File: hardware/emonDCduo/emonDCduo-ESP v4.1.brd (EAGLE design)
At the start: 114.3 x 76.5 mm, 120 parts, among them IC1 ACS750LCA-050, IC2 ACS750LCA-050, Y1 32Khz

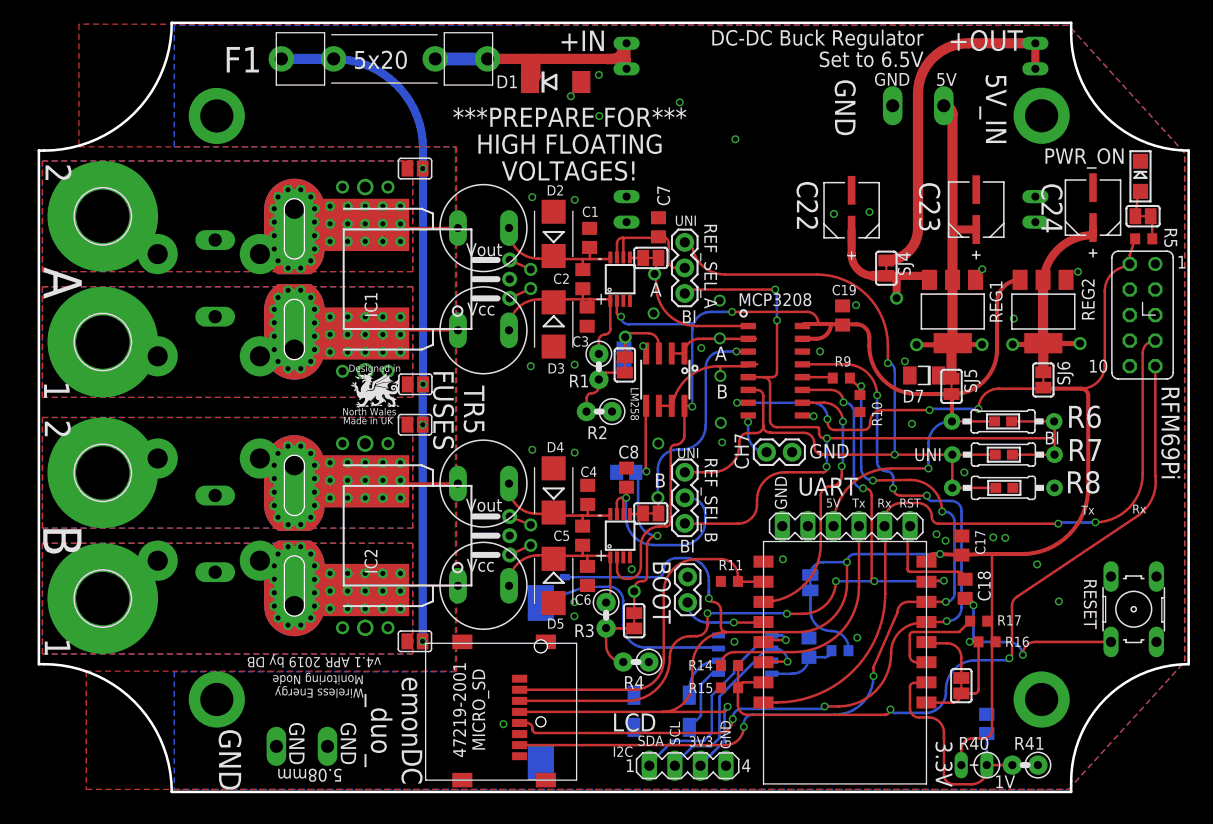
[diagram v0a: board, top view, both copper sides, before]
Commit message: commit v4.1
HV isolation improvements
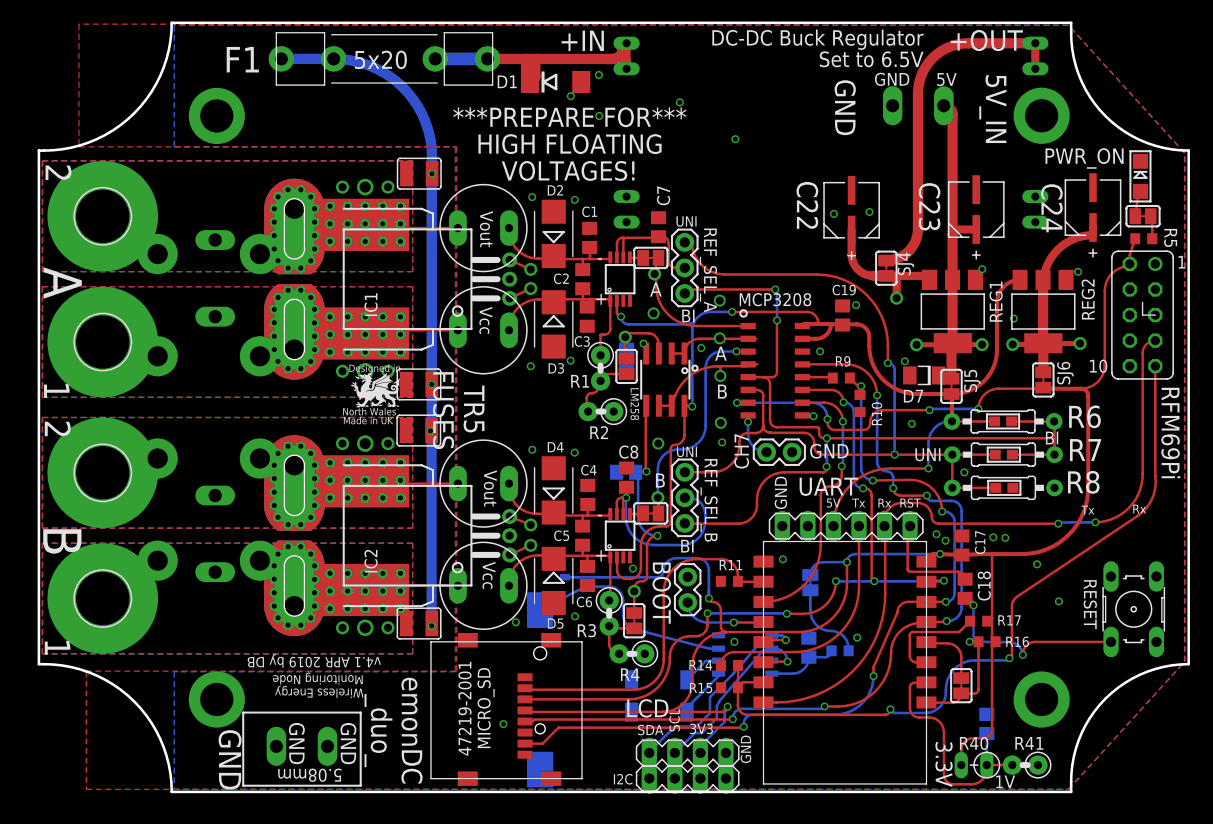
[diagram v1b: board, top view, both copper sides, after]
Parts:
- added SV2: (no value), con-lstb:MA04-1
- SJ1, SJ14, SJ3, SJ7: device jumper:SJ -> jumper:SJW
- moved SJ7 1.81 mm to (31.4, 18.5)
- moved Y1 1.53 mm to (55.3, 11.3)
- moved SV1 1.27 mm to (58.1, 5.65)
- moved R4 0.91 mm to (52.6, 15.5)
- moved CR1220 0.70 mm to (43.5, 11.6)
- moved SJ14 0.69 mm to (31.4, 37.7)
- moved SJ1 0.66 mm to (31.5, 63.2)
- moved MICRO_SD 0.55 mm to (44.6, 3.10)
- moved R3 0.37 mm to (50.3, 19.5)
- moved SJ3 0.36 mm to (31.4, 42.3)
- moved C21 0.28 mm to (52.1, 44.8)
- moved SJ8 0.22 mm to (52.1, 44.1)
- moved R1 0.22 mm to (49.5, 43.9)
- moved R2 0.17 mm to (49.5, 39.6)
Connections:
- net +3V3: now also SV2.3
- net GND: now also SV2.4
- net SCL: now also SV2.2
- net SDA: now also SV2.1
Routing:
- net N$45: track 6.97 -> 5.17 mm
- net GPIO14: track 85.6 -> 84.1 mm
- net +3V3: track 201.0 -> 202.5 mm
- net V_IN_PREFUSE: track 67.1 -> 65.7 mm
- net VSENSE_B: track 7.19 -> 6.14 mm
- net SDA: track 23.9 -> 24.6 mm
- net VBAT: track 21.9 -> 21.3 mm
- net N$44: track 4.63 -> 4.01 mm
- net GPIO12: track 81.2 -> 80.7 mm
- net GPIO13: track 73.5 -> 72.9 mm
- net SCL: track 21.5 -> 22.0 mm

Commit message: commit
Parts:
- SV1, SV2: device con-lstb:MA04-1 -> con-lstb-db:MA04-1
- moved R25 2.84 mm to (92.0, 37.3)
- moved R26 2.84 mm to (92.1, 34.0)
- moved R6 2.84 mm to (92.0, 37.3)
- moved R7 2.84 mm to (92.1, 34.0)
- moved R8 2.84 mm to (92.1, 30.7)
- moved R27 2.84 mm to (92.2, 30.7)
- moved U$4 2.36 mm to (55.2, 21.8)
- moved SJ9 2.15 mm to (55.0, 19.0)
- moved R3 1.96 mm to (52.3, 19.4)
- moved SJ7 1.52 mm to (31.4, 20.0)
- moved R4 1.46 mm to (54.1, 15.6)
- moved C17 1.27 mm to (86.7, 26.3)
- moved C18 1.27 mm to (87.0, 22.0)
- moved BOOT 1.27 mm to (59.4, 23.2)
- moved SV1 1.27 mm to (59.4, 5.65)
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- renumbered REG1 to REG1_5V, REG2 to REG2_3.3
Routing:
- net VBAT: track 21.3 -> 30.8 mm, vias 0 -> 2
- net +5V: track 116.7 -> 121.6 mm
- net UNI_REF: track 83.2 -> 86.7 mm
- net BI_REF: track 85.9 -> 88.6 mm
- net GPIO14: track 84.1 -> 86.3 mm
- net V_IN_PREFUSE: track 65.7 -> 64.0 mm
- net +3V3: track 202.5 -> 204.2 mm
- net GPIO12: track 80.7 -> 82.3 mm
- net GPIO13: track 72.9 -> 74.2 mm
- net D1/TX: track 73.0 -> 72.1 mm
- net D0/RX: track 67.0 -> 66.2 mm
- net SOURCE-POS-A_T: track 20.9 -> 20.1 mm
- net SOURCE-POS-B_T: track 18.8 -> 19.6 mm
- net LOAD-NEG-A_T: track 14.6 -> 13.9 mm
- net VSENSE_B_TP: track 23.6 -> 23.0 mm
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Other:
- board text removed: "LCD"
